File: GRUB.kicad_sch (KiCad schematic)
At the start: 57 parts, among them J2 External Digital Controller, J3 Timer or foot switch, Q1 2N3904, Q2 2N3904, Q3 2N3904, Q5 2N3904, SW1 R_SWITCH, SW2 U_SWITCH, SW3 B_SWITCH, SW4 1) Focus 2) Safelight 3) Colo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, SW6 G_WITCH, U1 A009 BuckBlock or LDDS-HWB, U10 PC817, U11 PC817, U12 PC817, U2 A009 BuckBlock or LDDS-HWB, U3 A009 BuckBlock or LDDS-HWB, U4 PC817, U5 PC817, U6 A009 BuckBlock or LDDS-HWB, U7 PC817, U8 PC817, U9 PC817

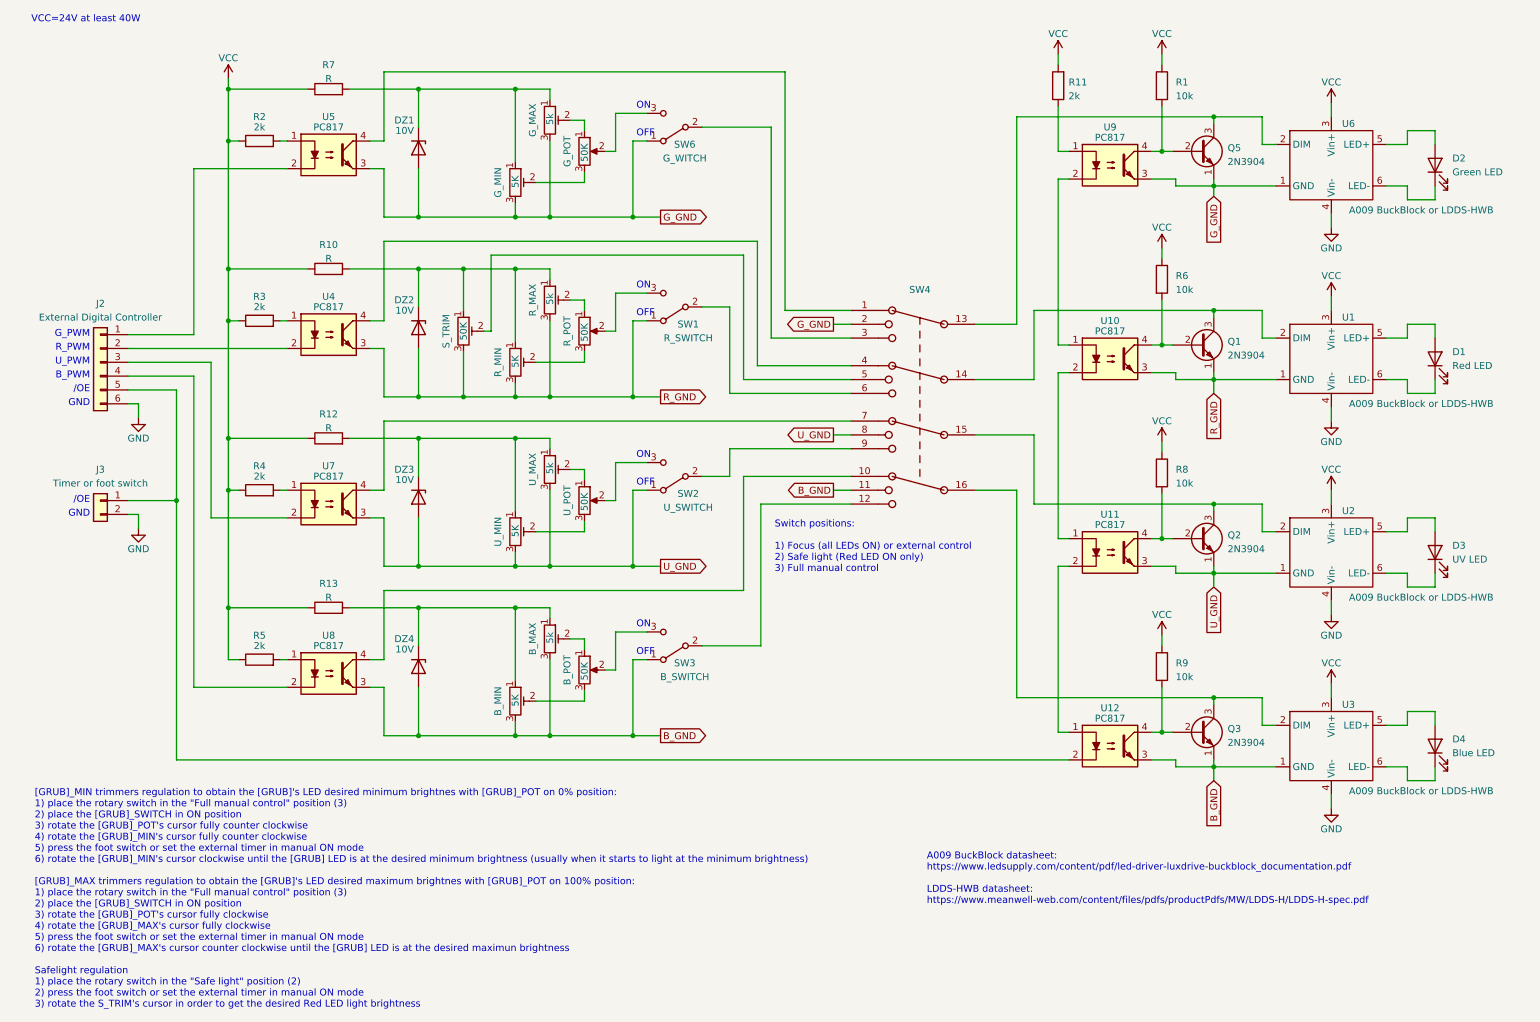
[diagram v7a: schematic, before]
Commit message: Adding connectors and separate power lines
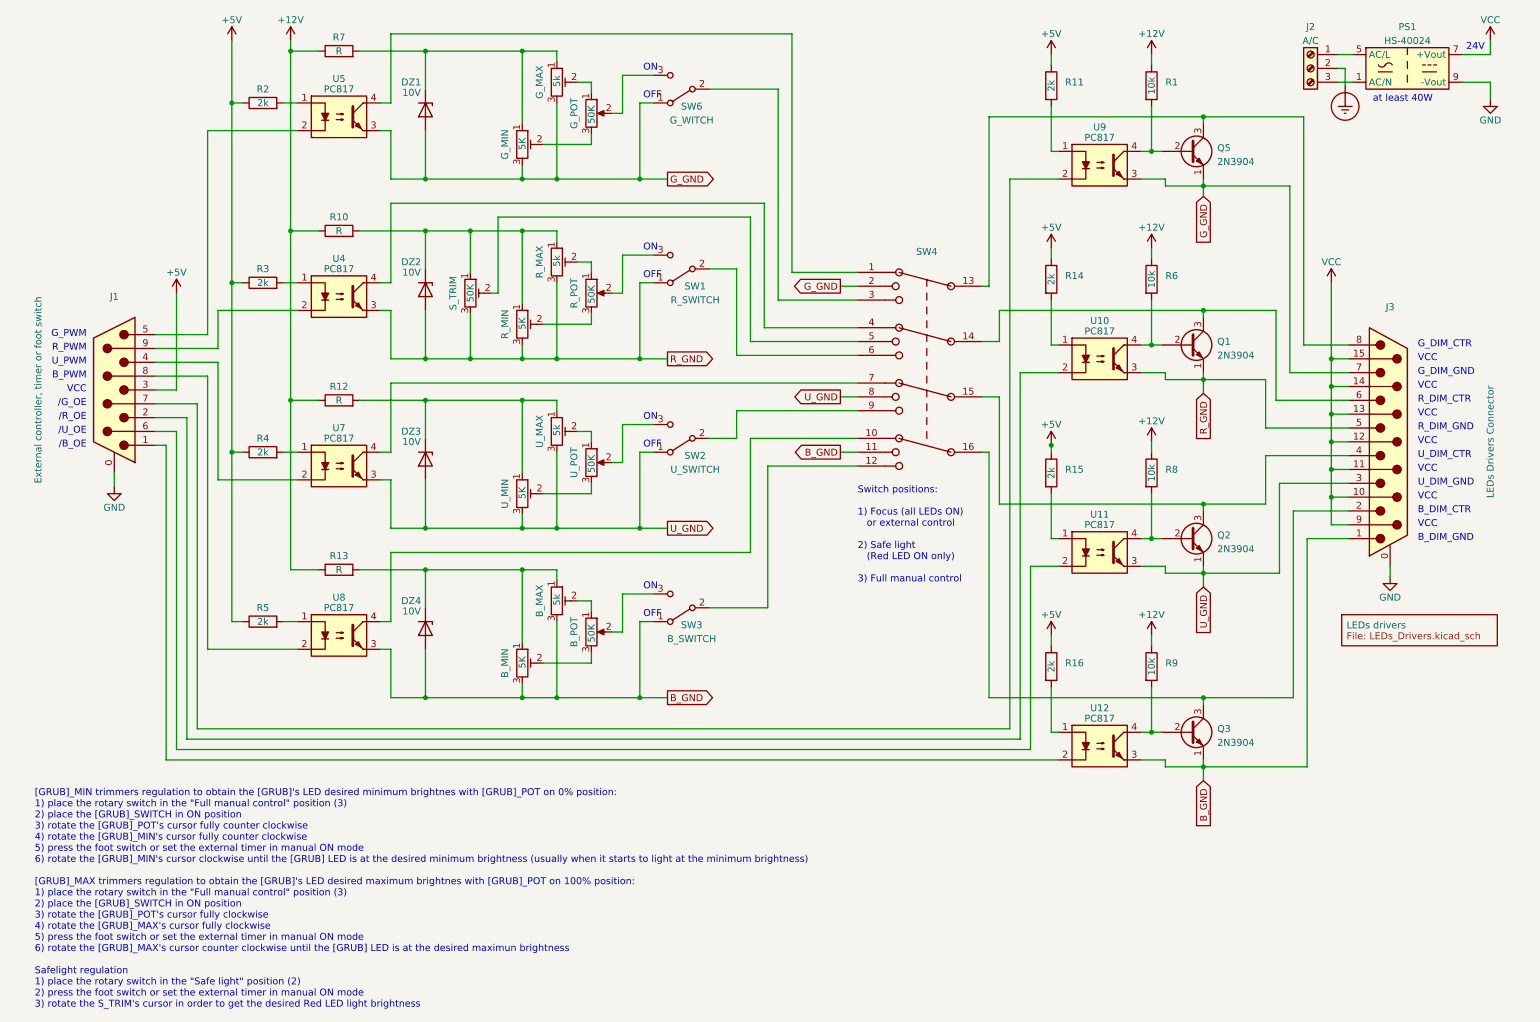
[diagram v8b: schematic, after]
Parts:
- removed D1: Red LED, symbol Device:LED
- removed D2: Green LED, symbol Device:LED
- removed D3: UV LED, symbol Device:LED
- removed D4: Blue LED, symbol Device:LED
- removed J2: External Digital Controller, symbol conn:Conn_01x06
- removed J3: Timer or foot switch, symbol conn:Conn_01x02
- removed U1, U2, U3, U6: A009 BuckBlock or LDDS-HWB, symbol LUXDrive:A009_BuckBlock
- added J1: External controller, timer or foot switch, symbol Connector:DB9_Male_MountingHoles
- added J2: A/C, symbol Connector:Screw_Terminal_01x03
- added J3: LEDs Drivers Connector, symbol Connector:DB15_Male_MountingHoles
- added PS1: HS-40024, Converter_ACDC:Converter_ACDC_Hahn_HS-400xx_THT, symbol Converter_ACDC:HS-40024
- added R14, R15, R16: 2k, symbol device:R
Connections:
- net B_GND: now also J3.1
- net GND: now also J1.0 (PAD), J3.0 (PAD), PS1.9 (-Vout)
- net G_GND: now also J3.7
- net R_GND: now also J3.5
- net U_GND: now also J3.3
- net VCC: now also J3.10 (P10), J3.11 (P111), J3.12 (P12), J3.13 (P13), J3.14 (P14), J3.15 (P15), J3.9 (P9), PS1.7 (+Vout); no longer R1.1, R10.1, R11.2, R12.1, R13.1, R2.1, R3.1, R4.1, R5.1, R6.1, R7.1, R8.1, R9.1
- net at U11.1: now also R15.2; no longer U10.2
- net at U11.2: now also J1.6; no longer U12.1
- net at U5.2: now also J1.5
- net at U4.2: now also J1.9
- net at U7.2: now also J1.4
- net at U8.2: now also J1.8
- net at U12.2: now also J1.1
- net at U9.1: now also R11.2; no longer R11.1
- net at Q5.3 (C), SW4.13: now also J3.8
- net at Q1.3 (C), SW4.14: now also J3.6
- net at Q2.3 (C), SW4.15: now also J3.4
- net at Q3.3 (C), SW4.16: now also J3.2
- net at U10.1: now also R14.2; no longer U9.2
- new net: R16.2, U12.1
- new net: J1.7, U9.2
- new net: J1.2, U10.2
- new net: J2.1 (Pin_1), PS1.5 (AC/L)
- new net: J2.3 (Pin_3), PS1.1 (AC/N)
- new net +12V: R1.1, R10.1, R12.1, R13.1, R6.1, R7.1, R8.1, R9.1
- new net +5V: J1.3, R11.1, R14.1, R15.1, R16.1, R2.1, R3.1, R4.1, R5.1
- new net Earth_Protective: J2.2 (Pin_2)
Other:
- added sheet LEDs drivers (LEDs_Drivers.kicad_sch)
- note added: "/B_OE"
- note added: "/G_OE"
- note added: "/R_OE"
- note added: "/U_OE"
- note added: "24V"
- note added: "B_DIM_CTR"
- note added: "B_DIM_GND"
- note added: "G_DIM_CTR"
- note added: "G_DIM_GND"
- note added: "R_DIM_CTR"
- note added: "R_DIM_GND"
- note added: "U_DIM_CTR"
- note added: "U_DIM_GND"
- note added: "VCC"
- note added: "at least 40W"
- note removed: "/OE"
- note removed: "A009 BuckBlock datasheet: https://www.ledsupply.com/content/pdf/led-driver-luxdrive-buckblock_documentation.pdf LDDS-HWB datasheet: https://www.meanwell-web.com/content/files/pdfs/productPdfs/MW/LDDS-H/LDDS-H-spec.pdf"
- note removed: "GND"
- note removed: "VCC=24V at least 40W"
- moved on the sheet: B_MAX, B_MIN, B_POT, DZ1, DZ2, DZ3, DZ4, G_MAX, G_MIN, G_POT, Q1, Q2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
